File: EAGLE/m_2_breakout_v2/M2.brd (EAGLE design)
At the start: 73.3 x 101.6 mm, 37 parts, among them X1 C-GRID-14-70543, X2 C-GRID-14-70543, X4 87758-0416

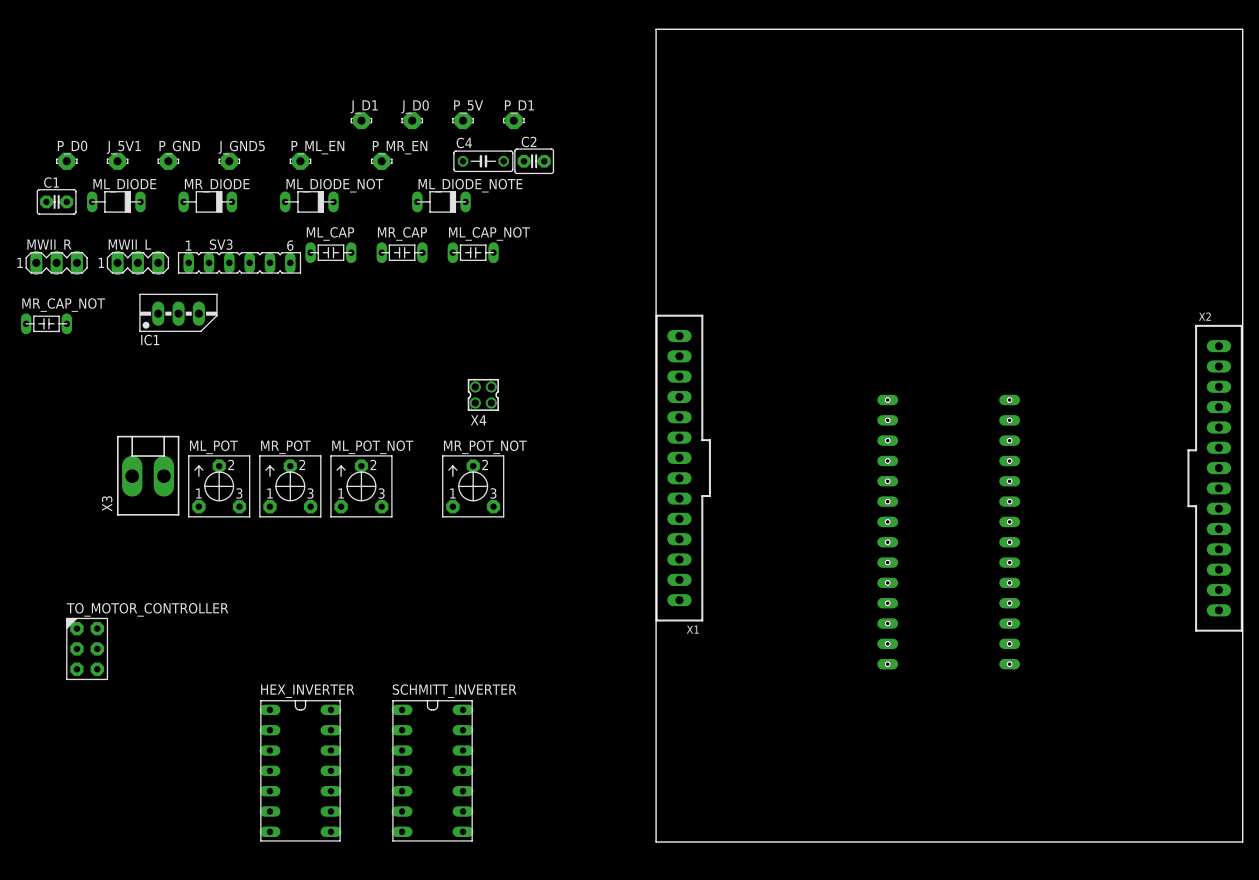
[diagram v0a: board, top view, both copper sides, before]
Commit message: Fixed everything about m2 board, just need optional switch rack
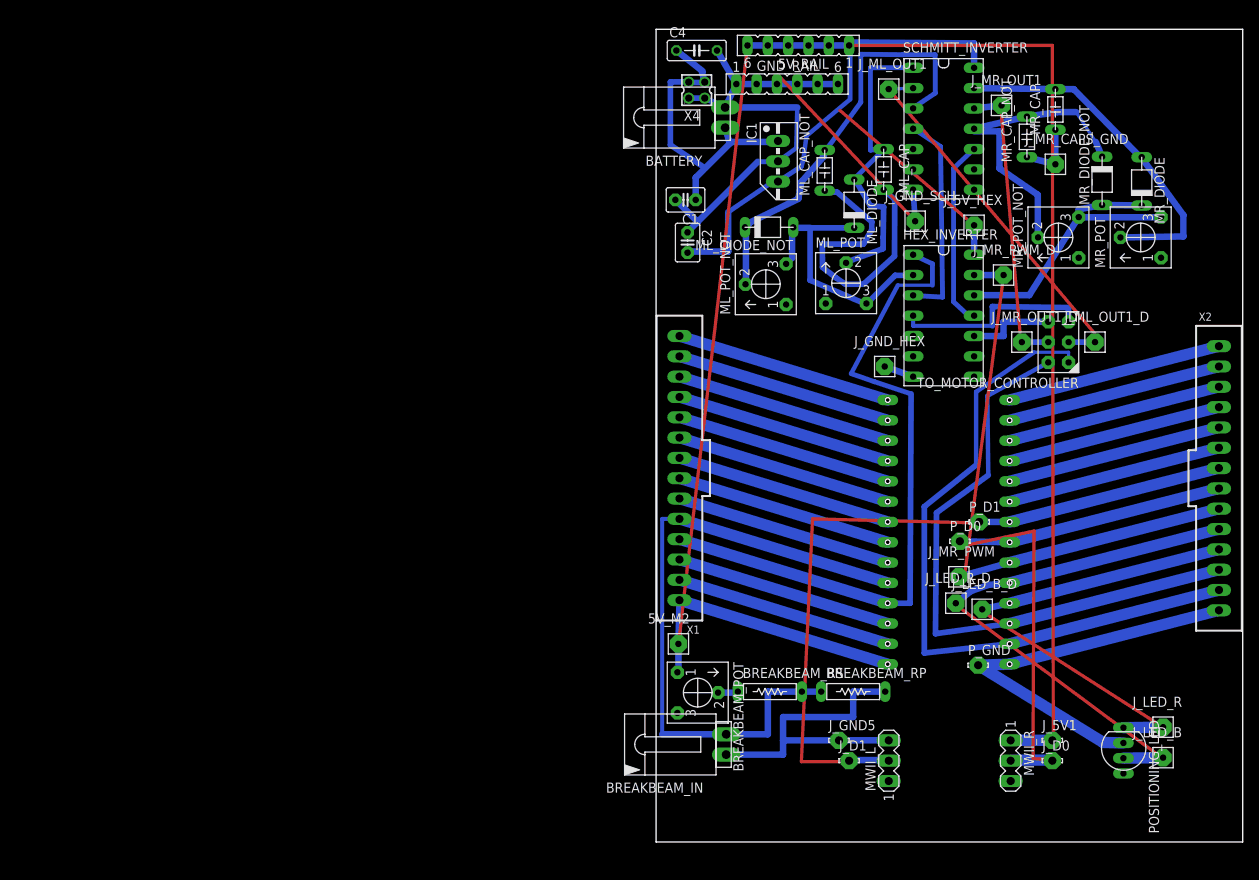
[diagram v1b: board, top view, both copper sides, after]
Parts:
- removed ML_DIODE_NOTE: 1N914B, ben_kramer:1N914B
- removed P_5V, P_ML_EN, P_MR_EN: LSP10, solpad:LSP10
- removed SV3: (no value), con-lsta:FE06
- removed X3: (no value), con-molex:KK-156-2
- added 5V_M2, J_5V_HEX, J_GND_HEX, J_GND_SCH, J_LED_B, J_LED_B_D, J_LED_R, J_LED_R_D, J_ML_OUT1, J_ML_OUT1_D, J_MR_CAPS_GND, J_MR_OUT1, J_MR_OUT1_D, J_MR_PWM, J_MR_PWM_D: ARDUINO_HEADER_1X1_OCTAGON, ben_kramer:ARDUINO_HEADER_1X1_OCTAGON
- added 5V_RAIL, GND_RAIL: (no value), con-lsta:FE06
- added BATTERY, BREAKBEAM_IN: MOLEX_2_PIN, ben_kramer:MOLEX_2_PIN
- added BREAKBEAM_POT: POTENTIOMETER_1, ben_kramer:POTENTIOMETER_1
- added BREAKBEAM_RP: 10k, ben_kramer:RESISTOR_THROUGH_8MM
- added BREAKBEAM_RS: 1k, ben_kramer:RESISTOR_THROUGH_8MM
- added MR_DIODE_NOT: 1N914B, ben_kramer:1N914B
- added POSITIONING_LED: RGB_LED, ben_kramer:RBG_LED
- moved J_5V1 137.4 mm to (49.5, 12.7)
- moved MWII_R 134.5 mm to (44.3, 10.2), turned to 270 degrees
- moved TO_MOTOR_CONTROLLER 127.3 mm to (50.3, 62.5), turned to 180 degrees
- moved MR_CAP_NOT 124.8 mm to (46.4, 88.1), turned to 90 degrees
- moved P_D0 121.3 mm to (38.0, 37.6)
- moved P_GND 119.2 mm to (40.3, 22.1)
- moved MR_DIODE 116.6 mm to (60.7, 82.4), turned to 270 degrees
- moved MR_POT 113.9 mm to (63.1, 75.6), turned to 90 degrees
- moved J_D0 113.2 mm to (49.5, 10.2)
- moved MWII_L 112.6 mm to (29.1, 10.2), turned to 90 degrees
- moved J_GND5 105.1 mm to (22.9, 12.7)
- moved SCHMITT_INVERTER 102.6 mm to (35.9, 89.2)
- moved J_D1 100.6 mm to (24.1, 10.2)
- moved HEX_INVERTER 98.5 mm to (35.9, 65.8)
- moved ML_DIODE 92.1 mm to (24.8, 79.6), turned to 270 degrees
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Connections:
- net N$3 renamed B5
- net N$6 renamed C7
- removed net GND_1: J_GND5.MP, MWII_L.3
- removed net N$14: C1.2, C2.1, IC1.GND
- removed net N$34: C1.1, C4.1, IC1.IN, X3.2, X4.2, X4.4
- removed net N$5: U$1.C6, X1.5
- removed net N$51: C4.2, SV3.1, SV3.2, SV3.3, SV3.4, SV3.5, SV3.6, X3.1, X4.1, X4.3
- new net 5V_HEX: HEX_INVERTER.14, J_5V_HEX.1
- new net BREAKBEAM_OUT: BREAKBEAM_IN.2, BREAKBEAM_RP.P$1, BREAKBEAM_RS.P$2, U$1.C6, X1.5
- new net GND_HEX: HEX_INVERTER.7, J_GND_HEX.1
- new net GND_SCH: J_GND_SCH.1, SCHMITT_INVERTER.7
- new net IN_GND: BATTERY.2, C1.2, C2.1, C4.2, GND_RAIL.1, GND_RAIL.2, GND_RAIL.3, GND_RAIL.4, GND_RAIL.5, GND_RAIL.6, IC1.GND, X4.1, X4.3
- new net LED_B: J_LED_B.1, POSITIONING_LED.B
- new net LED_R: J_LED_R.1, POSITIONING_LED.R
- new net M2_GND: BREAKBEAM_IN.1, BREAKBEAM_RP.P$2, J_GND5.MP, MWII_L.3
- new net ML_OUT1_D: J_ML_OUT1_D.1, TO_MOTOR_CONTROLLER.2
- new net MR_CAPS_GND: J_MR_CAPS_GND.1, MR_CAP.1, MR_CAP_NOT.1
- new net MR_OUT1_D: J_MR_OUT1_D.1, TO_MOTOR_CONTROLLER.5
- new net MR_PWM_D: HEX_INVERTER.13, J_MR_PWM_D.1
- new net N$19: 5V_M2.1, U$1.V+, X1.1
- new net N$6: BREAKBEAM_POT.2, BREAKBEAM_RS.P$1
- new net VIN: BATTERY.1, C1.1, C4.1, IC1.IN, X4.2, X4.4
- net 5V: now also 5V_RAIL.1, 5V_RAIL.2, 5V_RAIL.3, 5V_RAIL.4, 5V_RAIL.5, 5V_RAIL.6, BREAKBEAM_POT.1; no longer HEX_INVERTER.14, P_5V.MP, U$1.V+, X1.1
- net B2: now also J_LED_B_D.1
- net B3: now also J_LED_R_D.1
- net GND: no longer HEX_INVERTER.7, MR_CAP.1, MR_CAP_NOT.1, SCHMITT_INVERTER.7
- net ML_EN: no longer P_ML_EN.MP
- net ML_OUT1: now also J_ML_OUT1.1; no longer TO_MOTOR_CONTROLLER.2
- net MR_EN: no longer P_MR_EN.MP
- net MR_OUT1: now also J_MR_OUT1.1; no longer TO_MOTOR_CONTROLLER.5
- net MR_PWM: now also J_MR_PWM.1; no longer HEX_INVERTER.13
- net MR_PWM_NOT: now also MR_DIODE_NOT.+; no longer ML_DIODE_NOTE.+
- net N$17: now also POSITIONING_LED.GND
- net N$4: now also MR_DIODE_NOT.-; no longer ML_DIODE_NOTE.-
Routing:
- net 5V: track 0.00 -> 149.8 mm
- net N$31: track 0.00 -> 112.1 mm
- net ML_EN: track 0.00 -> 87.8 mm
- net ML_PWM: track 0.00 -> 86.3 mm
- net BREAKBEAM_OUT: track 0.00 -> 83.9 mm
- net MR_EN: track 0.00 -> 78.1 mm
- net IN_GND: track 0.00 -> 61.4 mm
- net N$18: track 0.00 -> 57.2 mm
- net ML_B2: track 0.00 -> 53.4 mm
- net N$17: track 0.00 -> 51.9 mm
- net N$1: track 0.00 -> 49.0 mm
- net ML_OUT1: track 0.00 -> 44.2 mm
- net M2_GND: track 0.00 -> 41.0 mm
- net VIN: track 0.00 -> 39.7 mm
- net N$4: track 0.00 -> 38.7 mm
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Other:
- board text added: "JUMPS SHOWN IN TOP LAYER D0 - MWii Right 2 D1 - mWii Left 2 5V- mwii right 1 GND - mwii right 3 M2_5V - 5V HEX_5V - 5V HEX_GND - GND SCHMITT_GND - GND MR_CAPS GND - GND MR_PWM - HEX_INV pin 13 SCHMITT_ML_OUT1 - MOTOR CONTROLLER OUT SCHMITT_MR_OUT1 - MOTOR CONTROLLER OUT M2_B2 - LED_BLUE M2_B3 - LED_RED"

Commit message: Fixed headers out
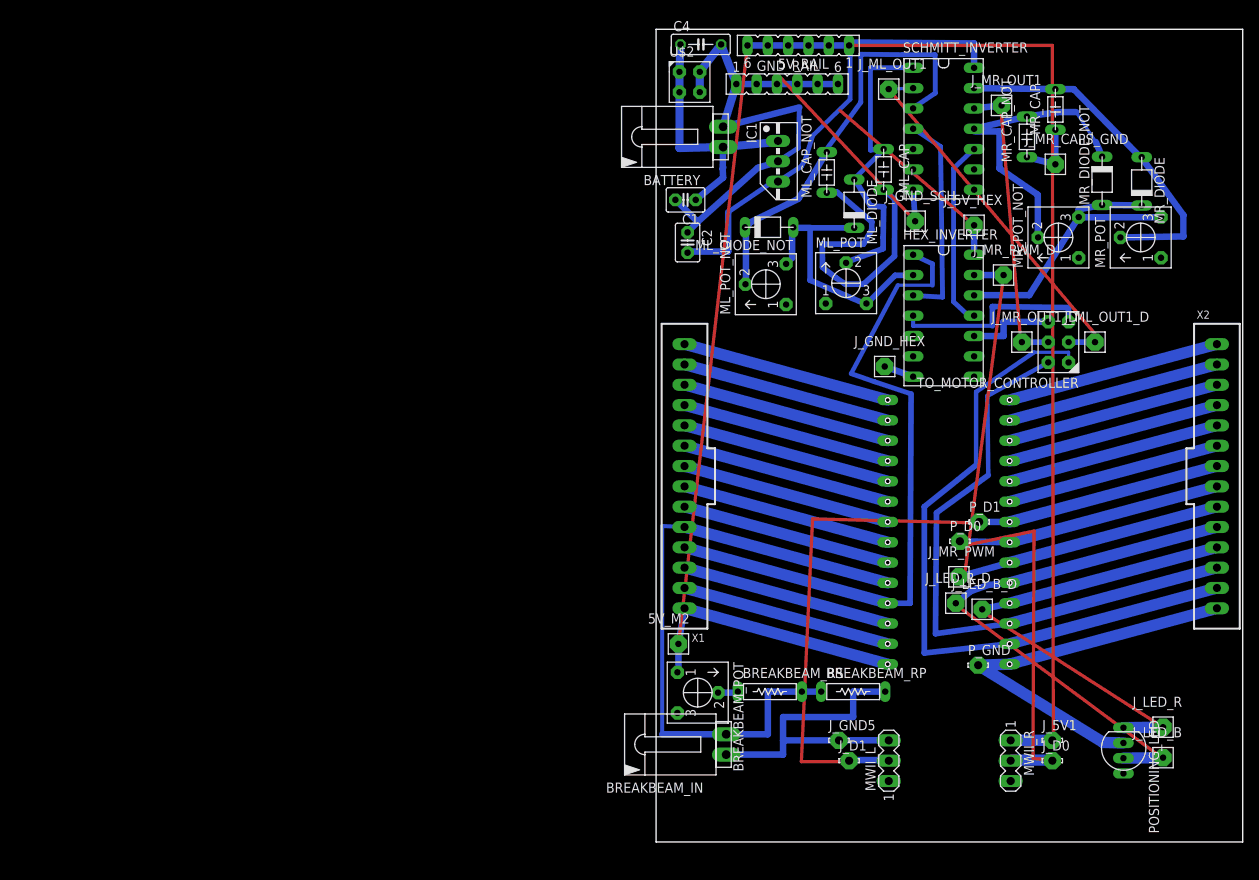
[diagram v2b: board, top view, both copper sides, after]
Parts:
- removed X4: 87758-0416, con-molex:87758-0416
- added U$2: ARDUINO_HEADER_2X2, ben_kramer:ARDUINO_HEADER_2X2
- moved BATTERY 2.43 mm to (2.03, 88.1)
- moved X1 1.20 mm to (3.56, 45.7)
- moved C4 0.92 mm to (5.59, 99.7)
- moved ML_CAP_NOT 0.36 mm to (21.3, 83.7)
- moved X2 0.36 mm to (70.1, 45.7)
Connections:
- net IN_GND: now also U$2.P3, U$2.P4; no longer X4.1, X4.3
- net VIN: now also U$2.P1, U$2.P2; no longer X4.2, X4.4
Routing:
- net VIN: track 39.7 -> 33.9 mm
- net IN_GND: track 61.4 -> 66.9 mm
- net N$19: track 32.7 -> 30.9 mm
- net BREAKBEAM_OUT: track 83.9 -> 82.8 mm
- net ML_PWM: track 86.3 -> 85.4 mm
- net N$15: track 27.2 -> 26.3 mm
- net N$13: track 27.2 -> 26.3 mm
- net C7: track 27.2 -> 26.3 mm
- net N$9: track 27.2 -> 26.3 mm
- net N$8: track 27.2 -> 26.3 mm
- net N$7: track 27.2 -> 26.3 mm
- net N$2: track 27.2 -> 26.3 mm
- net N$12: track 27.2 -> 26.3 mm
- net N$11: track 27.2 -> 26.3 mm
- net N$10: track 27.2 -> 26.3 mm
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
